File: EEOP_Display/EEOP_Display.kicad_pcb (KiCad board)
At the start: 2 copper layers, 2 parts, among them J1 Conn_01x32, J2 Conn_01x32

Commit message: Finished EEOP PCB
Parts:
- added REF**: MountingHole_2.2mm_M2, MountingHole:MountingHole_2.2mm_M2, F.Cu at (41.3, 23.5)
- added REF**: MountingHole_2.2mm_M2, MountingHole:MountingHole_2.2mm_M2, F.Cu at (28.7, 23.5)
- J1: value Conn_01x32 -> FH34SRJ-32S-0.5SH_50_; footprint Connector_FFC-FPC:Hirose_FH12-32S-0.5SH_1x32-1MP_P0.50mm_Horizontal -> Touchpoint:HRS_FH34SRJ-32S-0.5SH_50_
- moved J1 9.52 mm to (35.0, 18.5)
- moved J2 7.35 mm to (30.0, 40.0)
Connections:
- J1 pad 1: /E32 -> /E1
- J1 pad 10: /E23 -> /E10
- J1 pad 11: /E22 -> /E11
- J1 pad 12: /E21 -> /E12
- J1 pad 13: /E20 -> /E13
- J1 pad 14: /E19 -> /E14
- J1 pad 15: /E18 -> /E15
- J1 pad 16: /E17 -> /E16
- J1 pad 17: /E16 -> /E17
- J1 pad 18: /E15 -> /E18
- J1 pad 19: /E14 -> /E19
- J1 pad 2: /E31 -> /E2
- J1 pad 20: /E13 -> /E20
- J1 pad 21: /E12 -> /E21
- J1 pad 22: /E11 -> /E22
- J1 pad 23: /E10 -> /E23
- J1 pad 24: /E9 -> /E24
- J1 pad 25: /E8 -> /E25
- J1 pad 26: /E7 -> /E26
- J1 pad 27: /E6 -> /E27
- J1 pad 28: /E5 -> /E28
- J1 pad 29: /E4 -> /E29
- J1 pad 3: /E30 -> /E3
- J1 pad 30: /E3 -> /E30
- J1 pad 31: /E2 -> /E31
- J1 pad 32: /E1 -> /E32
- J1 pad 4: /E29 -> /E4
- J1 pad 5: /E28 -> /E5
- J1 pad 6: /E27 -> /E6
- J1 pad 7: /E26 -> /E7
- J1 pad 8: /E25 -> /E8
- J1 pad 9: /E24 -> /E9
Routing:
- net /E1: track 0.00 -> 29.3 mm, vias 0 -> 13
- net /E32: track 0.00 -> 28.2 mm, vias 0 -> 13
- net /E2: track 0.00 -> 28.0 mm, vias 0 -> 13
- net /E4: track 0.00 -> 27.2 mm, vias 0 -> 13
- net /E30: track 0.00 -> 26.9 mm, vias 0 -> 13
- net /E6: track 0.00 -> 26.4 mm, vias 0 -> 13
- net /E28: track 0.00 -> 23.6 mm, vias 0 -> 13
- net /E3: track 0.00 -> 22.7 mm, vias 0 -> 13
- net /E9: track 0.00 -> 22.0 mm, vias 0 -> 13
- net /E5: track 0.00 -> 21.6 mm, vias 0 -> 13
- net /E29: track 0.00 -> 21.2 mm, vias 0 -> 13
- net /E7: track 0.00 -> 20.9 mm, vias 0 -> 13
- net /E31: track 0.00 -> 20.9 mm, vias 0 -> 13
- net /E26: track 0.00 -> 20.7 mm, vias 0 -> 13
- net /E11: track 0.00 -> 20.5 mm, vias 0 -> 13
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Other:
- board outline added: 18 x 27 mm

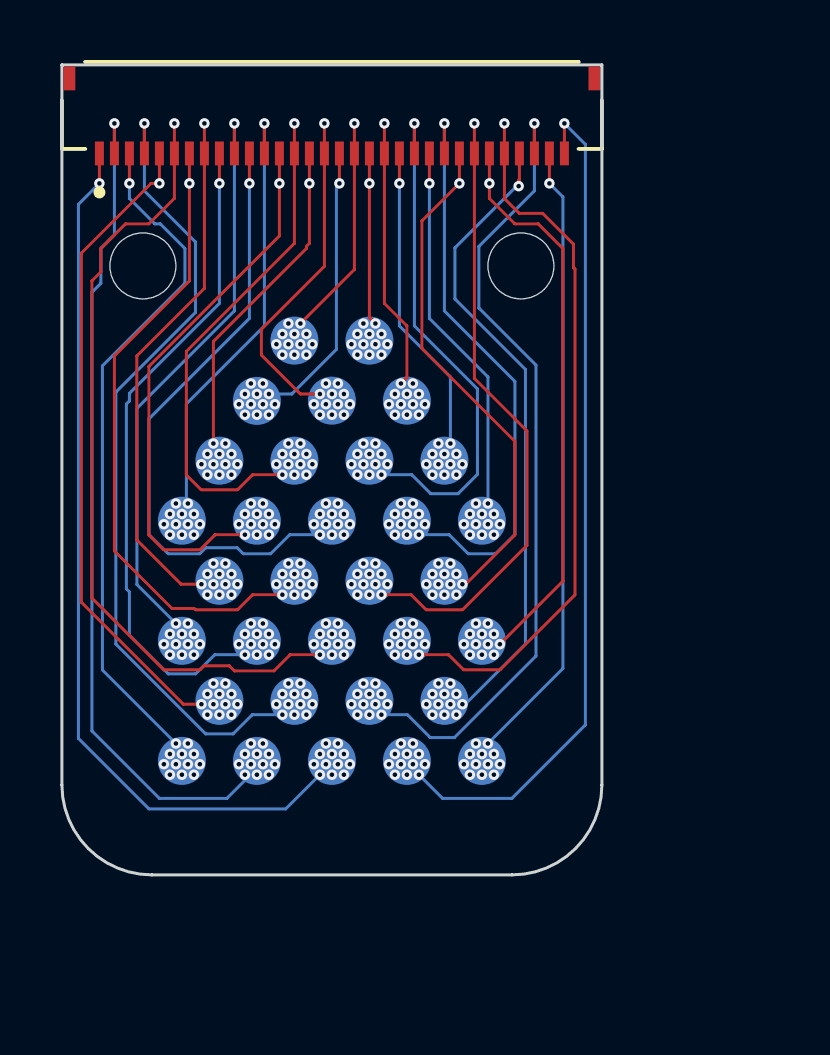
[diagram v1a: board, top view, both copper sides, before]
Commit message: Updated board outline slightly
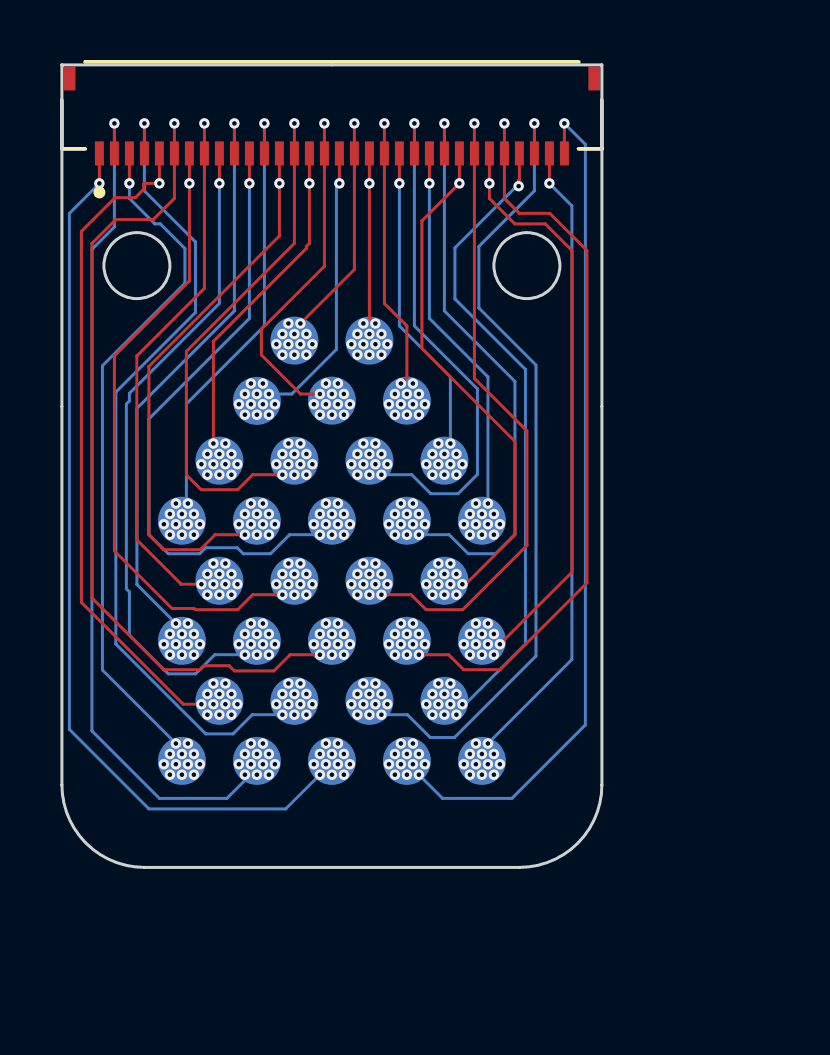
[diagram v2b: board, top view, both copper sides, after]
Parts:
- moved REF** 0.20 mm to (41.5, 23.5)
- moved REF** 0.20 mm to (28.5, 23.5)
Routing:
- net /E5: track 21.6 -> 22.1 mm
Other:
- board size 18 x 27 mm -> 18 x 26.7 mm

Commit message: Final changes for manufacturing
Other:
- board text added: "Carson R."
- board text added: "Touchpoint EEOP V1"

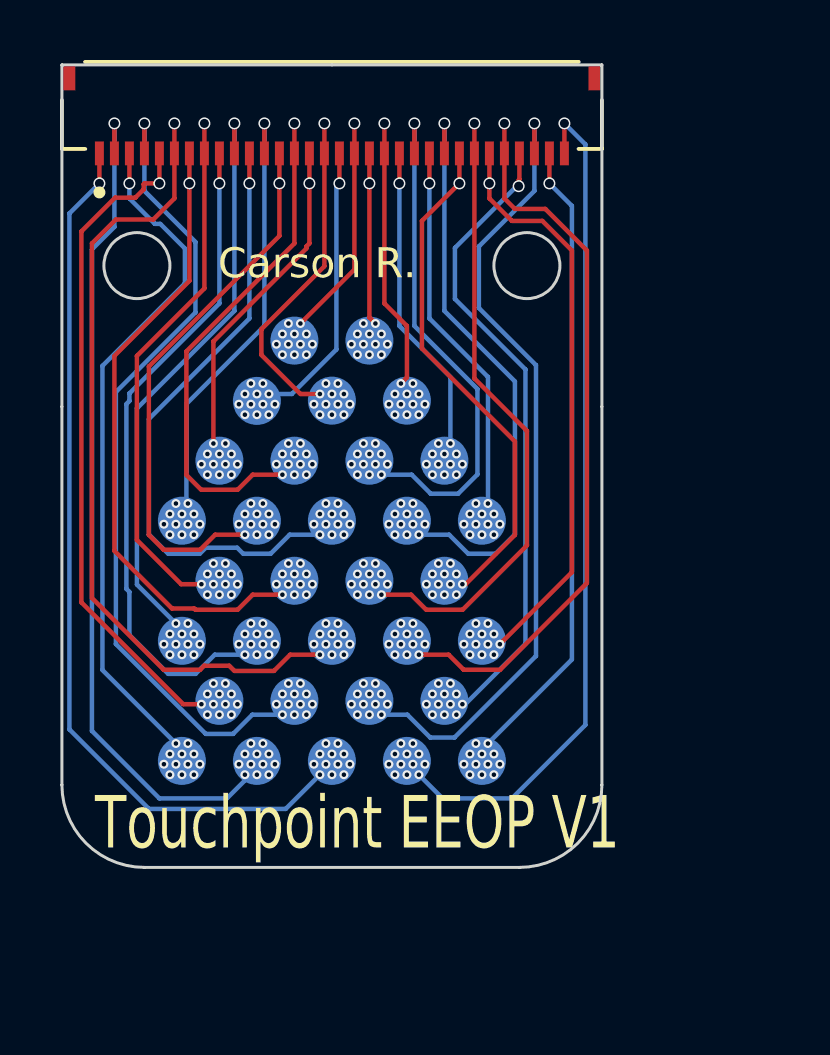
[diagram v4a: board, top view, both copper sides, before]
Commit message: Fixed EEOP via size
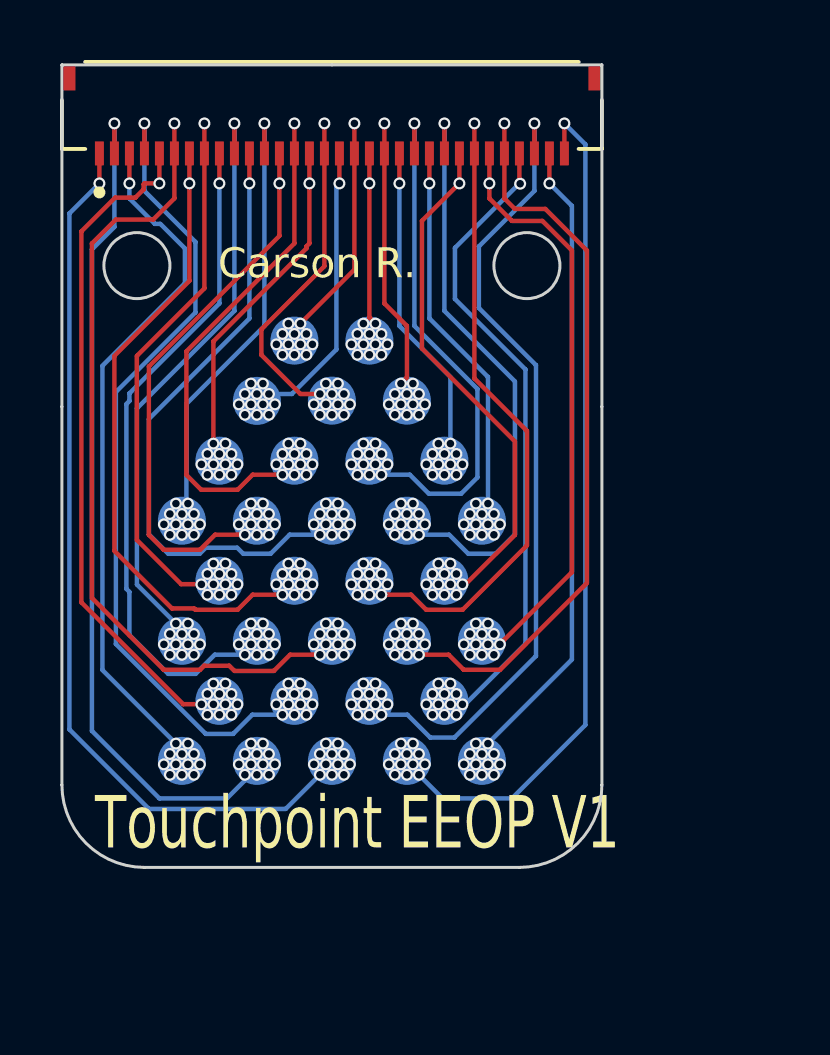
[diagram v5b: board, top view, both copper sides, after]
